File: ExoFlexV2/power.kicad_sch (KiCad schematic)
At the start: 17 parts

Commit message: Schematic structure
Ajout des Encodeur magnétique et load cells, début de circuit de comparateurs
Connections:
- net at PS?.3 (-Vout): now also J?.1 (Pin_1)
- net at PS?.4 (+Vout): now also FL?.4

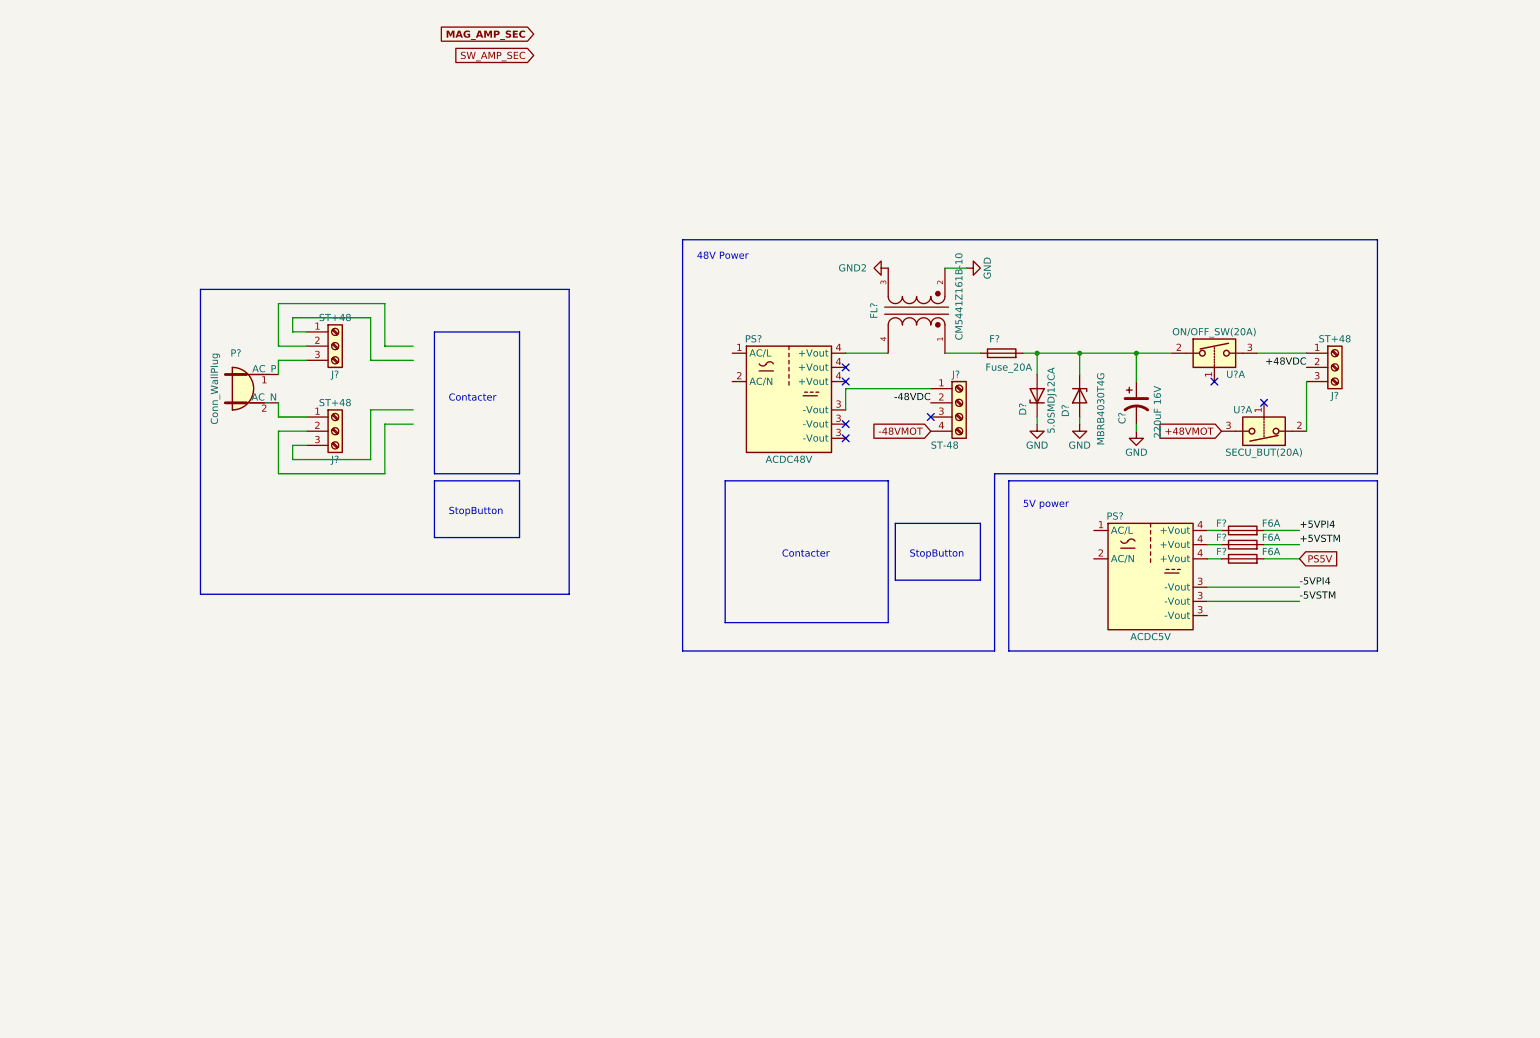
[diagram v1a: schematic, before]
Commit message: Many changes
Debouncing, power protection, potentiometer limits, etc.
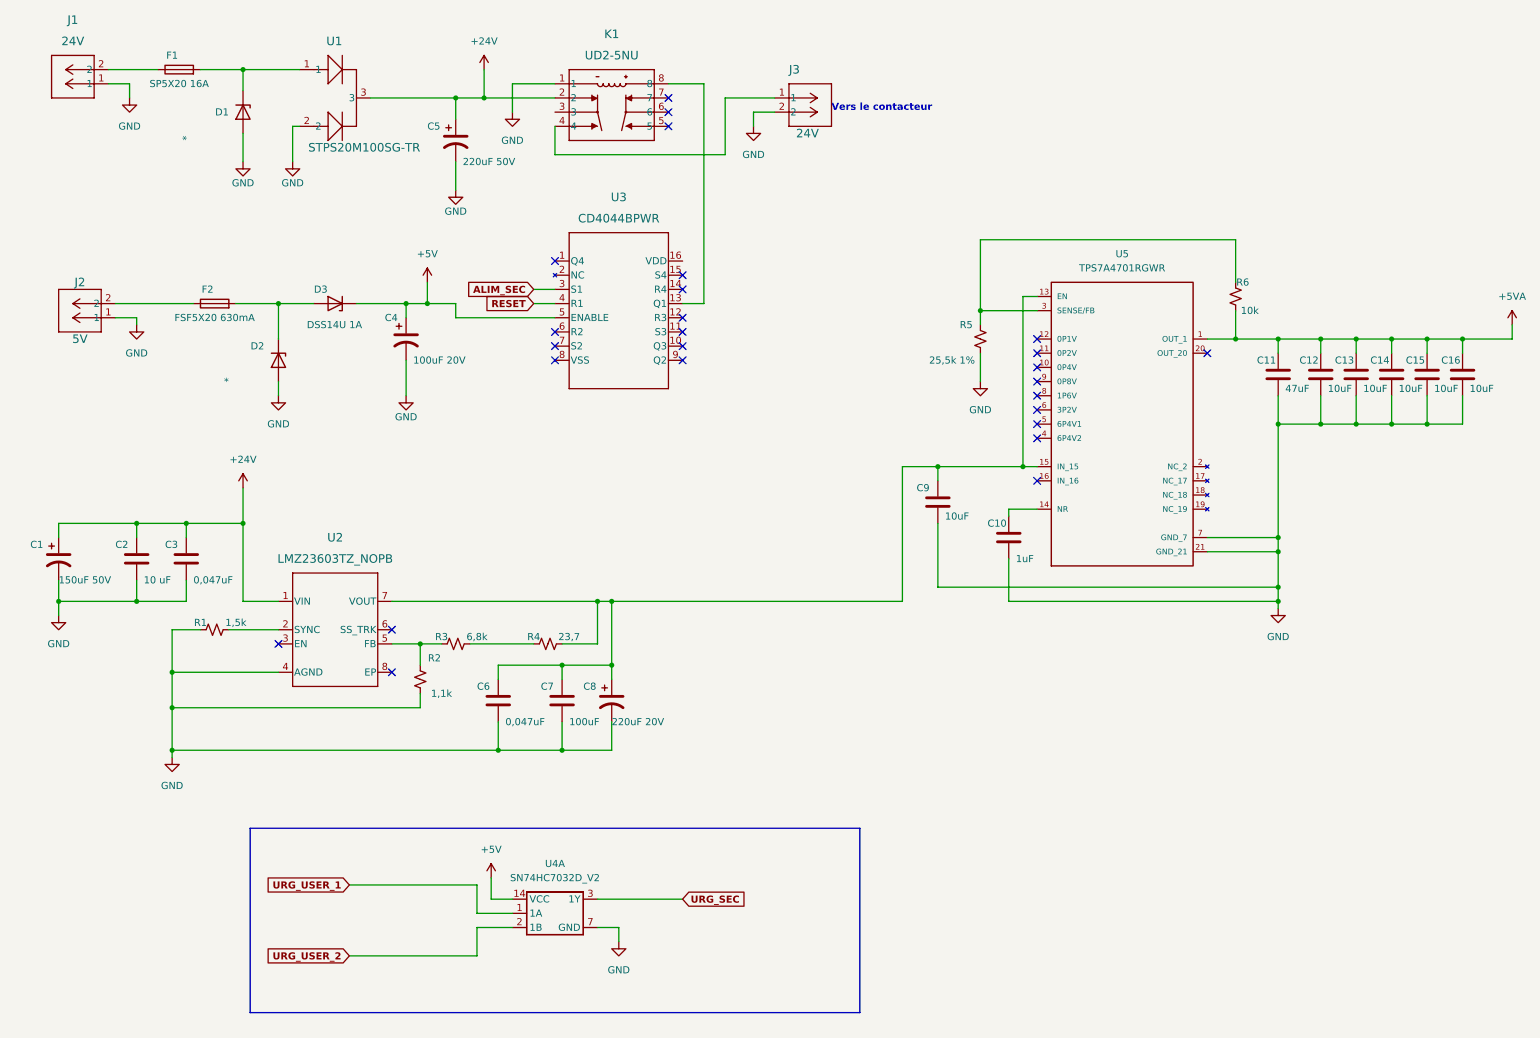
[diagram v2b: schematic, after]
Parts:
- removed C?: 220uF 16V, symbol Device:C_Polarized_US
- removed D?: MBRB4030T4G, symbol Device:D_Zener
- removed D?: 5.0SMDJ12CA, symbol Device:D_Zener
- removed F? (x3): F6A, symbol Device:Fuse
- removed F?: Fuse_20A, symbol Device:Fuse
- removed FL?: CM5441Z161B-10, FIL_CM5441Z161B-10, symbol CM5441Z161B-10:CM5441Z161B-10
- removed J? (x3): ST+48, symbol Connector:Screw_Terminal_01x03
- removed J?: ST-48, symbol Connector:Screw_Terminal_01x04
- removed P?: Conn_WallPlug, symbol Connector:Conn_WallPlug
- removed PS?: ACDC5V, Converter_ACDC:Converter_ACDC_HiLink_HLK-PMxx, symbol Converter_ACDC:HLK-PM01
- removed PS?: ACDC48V, Converter_ACDC:Converter_ACDC_HiLink_HLK-PMxx, symbol Converter_ACDC:HLK-PM01
- removed U?: SECU_BUT(20A), Package_SO:SOIC-16_3.9x9.9mm_P1.27mm, symbol Analog_Switch:DG308AxY
- removed U?: ON/OFF_SW(20A), Package_SO:SOIC-16_3.9x9.9mm_P1.27mm, symbol Analog_Switch:DG308AxY
- added C1: 150uF 50V, FootPrint:CAP_EEHZS1H151P, symbol Device:C_Polarized_US
- added C10: 1uF, Capacitor_SMD:C_0603_1608Metric, symbol Device:C
- added C11: 47uF, Capacitor_SMD:C_1206_3216Metric, symbol Device:C
- added C12, C13, C14, C15, C16, C9: 10uF, Capacitor_SMD:C_0603_1608Metric, symbol Device:C
- added C2: 10 uF, Capacitor_SMD:C_0805_2012Metric, symbol Device:C
- added C3, C6: 0,047uF, Capacitor_SMD:C_0603_1608Metric, symbol Device:C
- added C4: 100uF 20V, FootPrint:CAP_PC_8X7_NCH, symbol Device:C_Polarized_US
- added C5: 220uF 50V, FootPrint:CAP_EEHZS1H221P, symbol Device:C_Polarized_US
- added C7: 100uF, Capacitor_SMD:C_1210_3225Metric, symbol Device:C
- added C8: 220uF 20V, FootPrint:CAP_20SVPK220M, symbol Device:C_Polarized_US
- added D1, D2: *, symbol Device:D_Zener
- added D3: DSS14U 1A, FootPrint:SODFL3618X110N, symbol Device:D_Zener
- added F1: SP5X20 16A, symbol Device:Fuse
- added F2: FSF5X20 630mA, symbol Device:Fuse
- added J1, J3: 24V, FootPrint:TerminalBlock14AWG, symbol SymLib:1729128
- added J2: 5V, FootPrint:TerminalBlock14AWG, symbol SymLib:1729128
- added K1: UD2-5NU, FootPrint:UD2_NU_KEM-L, symbol SymLib:UD2-5NU
- added R1: 1,5k, Resistor_SMD:R_0603_1608Metric, symbol Device:R_Small_US
- added R2: 1,1k, Resistor_SMD:R_0603_1608Metric, symbol Device:R_Small_US
- added R3: 6,8k, Resistor_SMD:R_0603_1608Metric, symbol Device:R_Small_US
- added R4: 23,7, Resistor_SMD:R_0603_1608Metric, symbol Device:R_Small_US
- added R5: 25,5k 1%, Resistor_SMD:R_0603_1608Metric, symbol Device:R_Small_US
- added R6: 10k, Resistor_SMD:R_0603_1608Metric, symbol Device:R_Small_US
- added U1: STPS20M100SG-TR, FootPrint:D2PAK_STM, symbol SymLib:STPS20M100SG-TR
- added U2: LMZ23603TZ_NOPB, FootPrint:LMZ23603, symbol SymLib:LMZ23603TZ_NOPB
- added U3: CD4044BPWR, FootPrint:CD4044BPWR, symbol SymLib:CD4044BPWR
- added U4: SN74HC7032D_V2, FootPrint:SN74HC7032D, symbol SymLib:SN74HC7032D_V2
- added U5: TPS7A4701RGWR, FootPrint:TPS7A470, symbol SymLib:TPS7A4701RGWR
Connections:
- net GND: now also C1.2, C10.2, C11.2, C12.2, C13.2, C14.2, C15.2, C16.2, C2.2, C3.2, C4.2, C5.2, C6.2, C7.2, C8.2, C9.2, D1.2 (A), D2.2 (A), J1.1, J2.1, J3.2, K1.1, R1.1, R2.1, R5.1, U1.2, U2.4 (AGND), U4.7 (GND), U5.21 (GND_21), U5.7 (GND_7)
- new net: C6.1, C7.1, C8.1, C9.1, R4.2, U2.7 (VOUT), U5.13 (EN), U5.15 (IN_15)
- new net: R1.2, U2.2 (SYNC)
- new net: R2.2, R3.1, U2.5 (FB)
- new net: C10.1, U5.14 (NR)
- new net: R5.2, R6.2, U5.3 (SENSE/FB)
- new net: K1.8, U3.13 (Q1)
- new net: D2.1 (K), D3.2 (A), F2.2
- new net: J3.1, K1.4
- new net: F1.1, J1.2
- new net: D1.1 (K), F1.2, U1.1
- new net: F2.1, J2.2
- new net: R3.2, R4.1
- new net +24V: C1.1, C2.1, C3.1, C5.1, K1.2, U1.3, U2.1 (VIN)
- new net +5V: C4.1, D3.1 (K), U3.5 (ENABLE), U4.14 (VCC)
- new net +5VA: C11.1, C12.1, C13.1, C14.1, C15.1, C16.1, R6.1, U5.1 (OUT_1)
- new net ALIM_SEC: U3.3 (S1)
- new net RESET: U3.4 (R1)
- new net URG_SEC: U4.3 (1Y)
- new net URG_USER_1: U4.1 (1A)
- new net URG_USER_2: U4.2 (1B)
- no-connect marks 7 -> 26
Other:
- note added: "Vers le contacteur"
- note removed: "48V Power"
- note removed: "5V power"
- note removed: "Contacter"
- note removed: "StopButton"

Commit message: quque truc
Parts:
- removed D2: *, symbol Device:D_Zener
- removed D3: DSS14U 1A, FootPrint:SODFL3618X110N, symbol Device:D_Zener
- added D2: DSS12UTR, FootPrint:SODFL3618X110N, symbol SymLib:DSS12UTR
- added TP1, TP2, TP3, TP4, TP5: 5005, FootPrint:KEYSTONE_5005, symbol SymLib:5005
- added U1: PTSM36ADBZR, SOT-23-3_DBZ_TEX, symbol SymLib:PTSM36ADBZR
- D1: value * -> TPD1E; footprint (none) -> FootPrint:DPY2_TEX
- F1, F2: footprint (none) -> FootPrint:696108003002
- renumbered U1 to U2, U2 to U3, U3 to U4, U4 to U5, U5 to U6
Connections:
- net +24V: now also TP2.TP
- net +5V: now also D2.1, TP1.TP
- net +5VA: now also TP5.TP
- net GND: now also U1.1 (GND), U1.2 (GND)
- net at C6.1, C7.1, C8.1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: now also TP4.TP
- net at F2.2: now also D1.1 (K), D2.2
- net at J3.1, K1.4: now also TP3.TP
- net at F1.2, U2.1: now also U1.3 (IO); no longer D1.1 (K)

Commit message: Placement
Début du placement et modification d'après dernier review
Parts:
- removed D2: DSS12UTR, FootPrint:SODFL3618X110N, symbol SymLib:DSS12UTR
- removed U5: SN74HC7032D_V2, FootPrint:SN74HC7032D, symbol SymLib:SN74HC7032D_V2
- added CR1: 1SS321_LF, FootPrint:1SS321_LF, symbol SymLib:1SS321_LF
- added CR2: TBAT54_LM, FootPrint:TBAT54_LM, symbol SymLib:TBAT54_LM
- added D2: SS12P2L-M3_86A, FootPrint:DIO_SS12P2L-M3_86A, symbol SymLib:SS12P2L-M3_86A
- added R4: RE1C002UNTCL, FootPrint:DIO_RB558WMF_ROM, symbol SymLib:RE1C002UNTCL
- added TP2, TP4, TP5, TP8: 5005, FootPrint:KEYSTONE_5005, symbol SymLib:5005
- F1: value SP5X20 16A -> FSF5X20 200mA
- F2: value FSF5X20 630mA -> FSF5X20 500mA
- renumbered R4 to R5, R5 to R6, R6 to R7, TP2 to TP3, TP3 to TP6, TP4 to TP7, TP5 to TP9, U4 to U3, U3 to U4, U6 to U5
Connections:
- net +24V: now also F1.2, U1.3 (IO)
- net +5V: now also D1.1 (K), F2.2, K1.8, U3.16 (VDD), CR1.3 (C), D2.3
- net ALIM_SEC: now also TP4.TP
- net GND: now also U2.1, U3.8 (VSS), CR2.1 (A), D2.1, D2.2, R4.2 (S); no longer K1.1
- net RESET: now also TP2.TP
- net LATCH_Q1: now reaches U3.13 (Q1)
- net LATCH_Q1: now also R4.1 (G), TP5.TP; no longer K1.8
- net 5V_IN: now reaches F2.1, J2.2
- net 24V_OUT: now reaches J3.1, K1.4, TP6.TP
- net 24V_OUT: now also CR2.3 (C)
- net 24V_IN: now reaches F1.1, J1.2
- new net COIL-: CR1.1 (A), CR1.2 (A), K1.1, R4.3 (D), TP8.TP
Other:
- moved on the sheet: C1, C10, C11, C12, C13, C14, C15, C16, C2, C3, C4, C5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

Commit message: Placement encore
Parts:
- added C1: 10uF, Capacitor_SMD:C_0603_1608Metric, symbol Device:C
- added R1: 5k, Resistor_SMD:R_0603_1608Metric, symbol Device:R_Small_US
- added TP131: 5005, FootPrint:KEYSTONE_5005, symbol SymLib:5005
- added U3: 74LV244PW, FootPrint:DB20, symbol SymLib:74LV244PW
- renumbered C9 to C10, C10 to C11, C11 to C12, C12 to C13, C13 to C14, C14 to C15, C15 to C16, C16 to C17, C1 to C2, C2 to C3, C3 to C4, C4 to C5, C5 to C6, C6 to C7, C7 to C8, C8 to C9, R1 to R2, R2 to R3, R3 to R4, R4 to R5, R5 to R6, R6 to R7, R7 to R8, U3 to U4, U4 to U5, U5 to U6
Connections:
- net GND: now also C1.2
- net RESET: now also R1.1; no longer TP2.TP, U4.4 (R1)
- new net: TP131.TP, TP2.TP, U3.16 (1Y1), U4.4 (R1)
- new net: C1.1, R1.2, U3.4 (1A1)

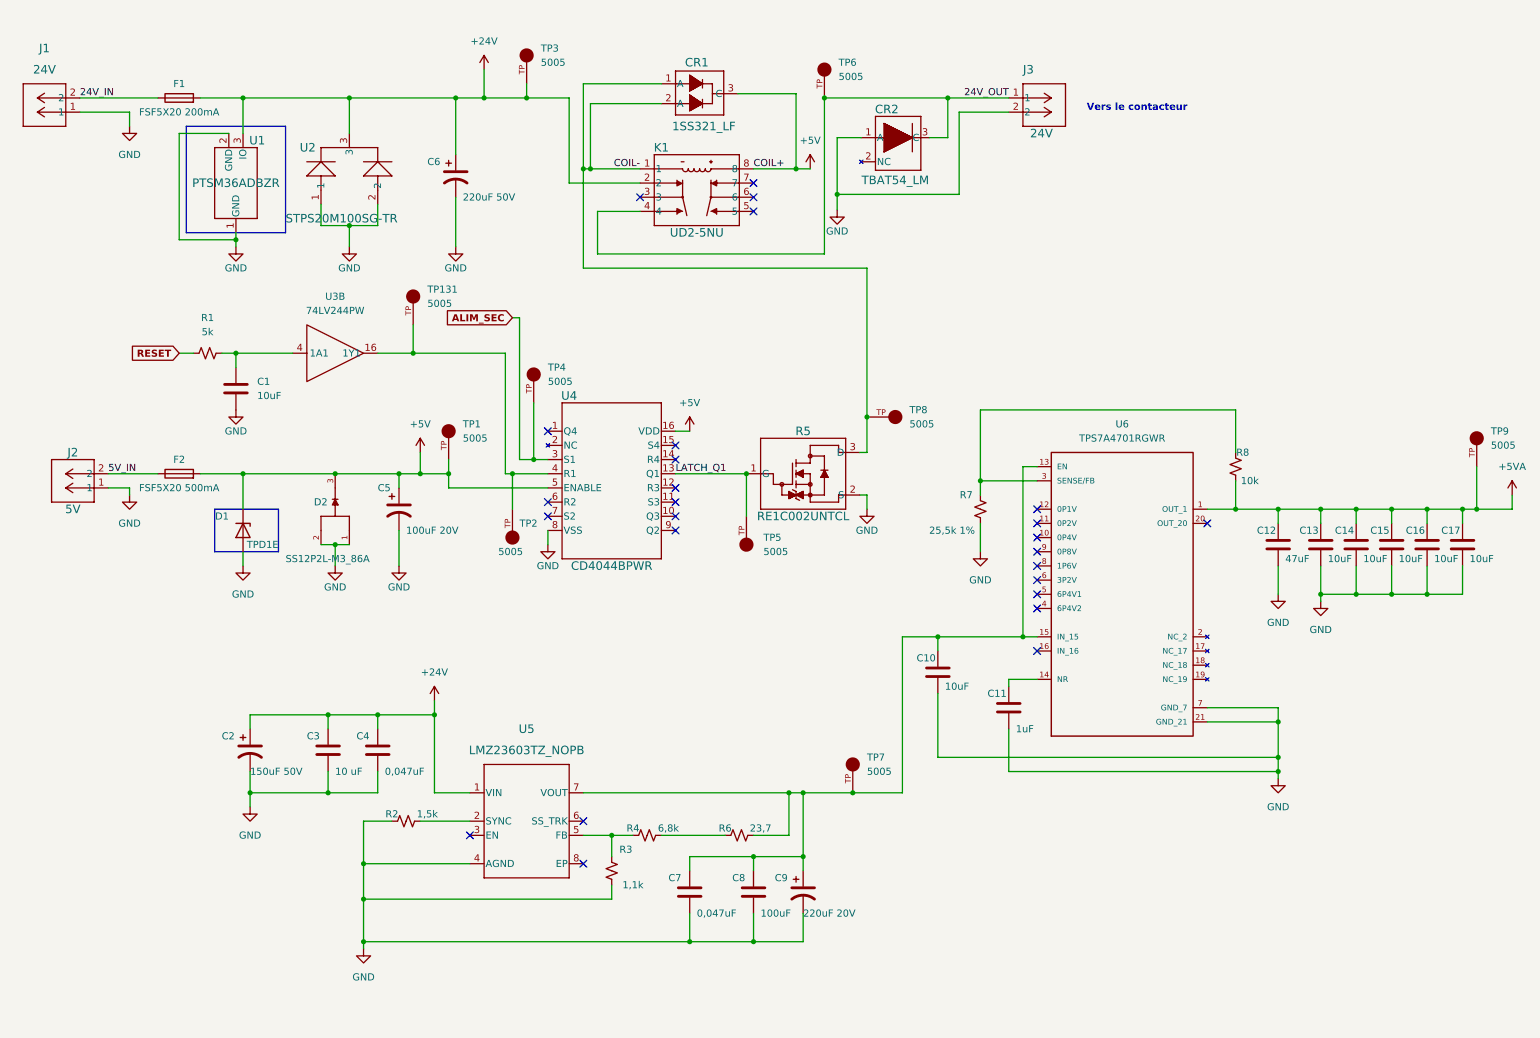
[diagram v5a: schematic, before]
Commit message: Mise à jour mi-stage
- Torque et Amplitude testé et vérifié
- Capteur de présence et de proximité testé
- Système de détection de coupure de fils
- Polyvalence pour plusieurs capteurs
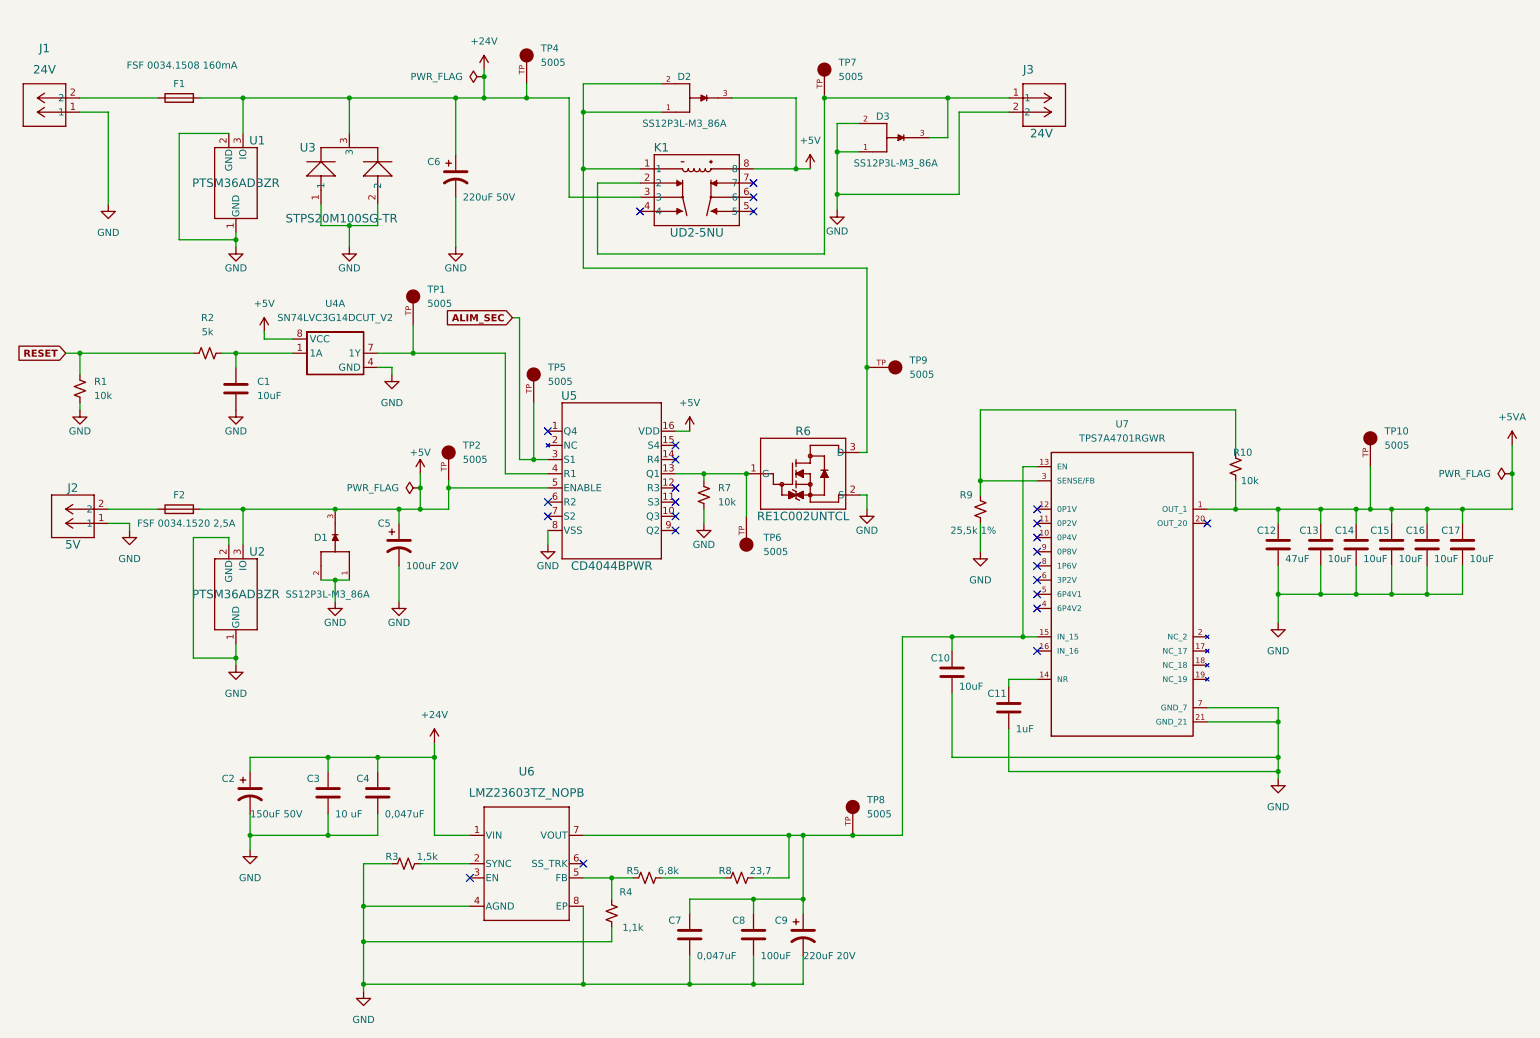
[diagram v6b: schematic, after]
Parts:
- removed CR1: 1SS321_LF, FootPrint:1SS321_LF, symbol SymLib:1SS321_LF
- removed CR2: TBAT54_LM, FootPrint:TBAT54_LM, symbol SymLib:TBAT54_LM
- removed D1: TPD1E, FootPrint:DPY2_TEX, symbol Device:D_Zener
- removed TP2: 5005, FootPrint:KEYSTONE_5005, symbol SymLib:5005
- removed U3: 74LV244PW, FootPrint:DB20, symbol SymLib:74LV244PW
- added D2, D3: SS12P3L-M3_86A, FootPrint:DIO_SS12P2L-M3_86A, symbol SymLib:SS12P2L-M3_86A
- added R1, R7: 10k, Resistor_SMD:R_0603_1608Metric, symbol Device:R_Small_US
- added U2: PTSM36ADBZR, FootPrint:SOT-23-3_DBZ_TEX, symbol SymLib:PTSM36ADBZR
- added U4: SN74LVC3G14DCUT_V2, FootPrint:SN74LVC3G14DCUT, symbol SymLib:SN74LVC3G14DCUT_V2
- D1: renamed from D2; value SS12P2L-M3_86A -> SS12P3L-M3_86A
- F1: value FSF5X20 200mA -> FSF 0034.1508 160mA
- F2: value FSF5X20 500mA -> FSF 0034.1520 2,5A
- U1: footprint SOT-23-3_DBZ_TEX -> FootPrint:SOT-23-3_DBZ_TEX
- renumbered R8 to R10, R1 to R2, R2 to R3, R3 to R4, R4 to R5, R5 to R6, R6 to R8, R7 to R9, TP131 to TP1, TP9 to TP10, TP1 to TP2, TP3 to TP4, TP4 to TP5, TP5 to TP6, TP6 to TP7, TP7 to TP8, TP8 to TP9, U2 to U3, U4 to U5, U5 to U6, U6 to U7
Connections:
- net +24V: now also K1.3; no longer K1.2
- net +5V: now also D2.3, U2.3 (IO), U4.8 (VCC)
- net GND: now also U6.8 (EP), D3.1, D3.2, R1.2, R7.1, U2.1 (GND), U2.2 (GND), U4.4 (GND)
- net RESET: now also R1.1
- net at TP1.TP, U5.4 (R1): now also U4.7 (1Y)
- net at C1.1, R2.2: now also U4.1 (1A)
- net 24V_IN: no longer names the net of F1.1, J1.2
- net 24V_OUT: no longer names the net of J3.1, TP7.TP
- net 24V_OUT: now also K1.2, D3.3; no longer K1.4
- net 5V_IN: no longer names the net of F2.1, J2.2
- net COIL-: no longer names the net of K1.1, R6.3 (D), TP9.TP
- net COIL-: now also D2.1, D2.2
- net LATCH_Q1: no longer names the net of R6.1 (G), TP6.TP, U5.13 (Q1)
- net LATCH_Q1: now also R7.2
- no-connect marks 26 -> 25
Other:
- note removed: "Vers le contacteur"
- moved on the sheet: C10, C2, C3, C4, C5, C7, C8, C9, D1, J2, R3, R4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
